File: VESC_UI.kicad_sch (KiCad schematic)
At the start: 60 parts, among them J1 Hall_DRV5055-Q1, J2 Hall_DRV5055-Q1, J3 Conn_01x07_Male, J4 Conn_02x05_Female, J5 Conn_01x05_Male, J6 Conn_01x04_Male, J8 Conn_01x02_Male, J9 Conn_01x02_Male, Q1 Mosfet IRLML2060TRPBF, Q2 Mosfet IRLML2060TRPBF, SW1 Vertical push button, SW2 Vertical push button, SW3 Vertical push button, SW4 Vertical push button, SW5 Push button, U2 STM32F401CEU6, U3 M95M04-DR

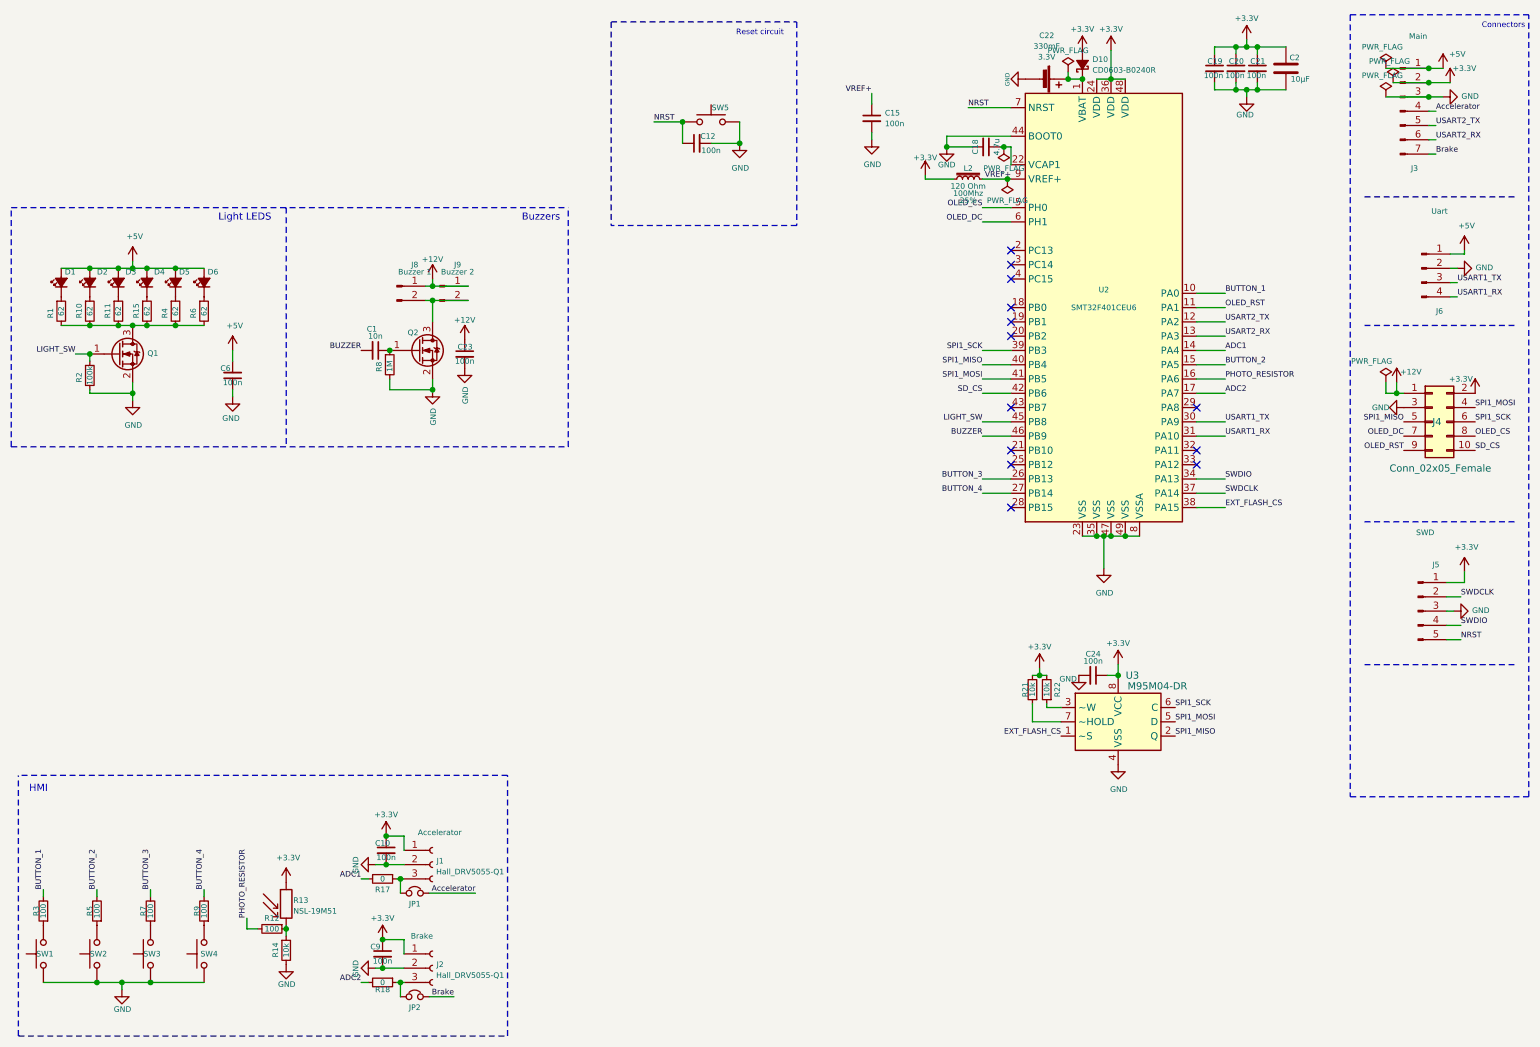
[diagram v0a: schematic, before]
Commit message: Merge display shield and update smd components case
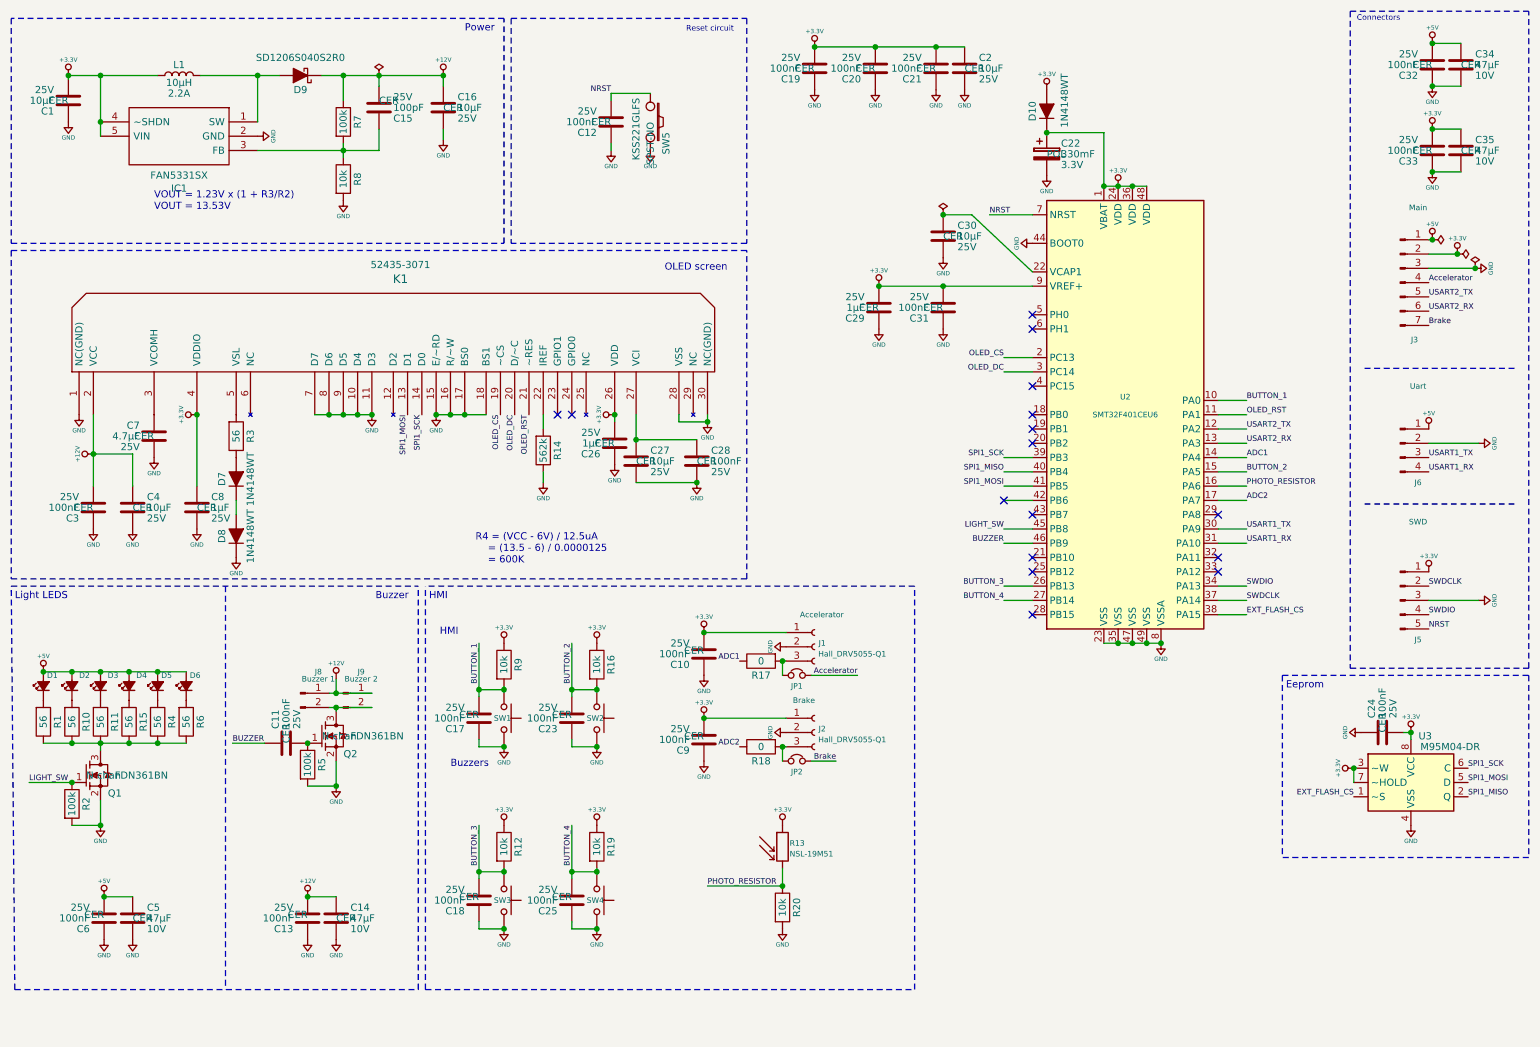
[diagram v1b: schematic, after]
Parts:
- removed C1: 10n, Capacitor_SMD:C_0603_1608Metric_Pad1.05x0.95mm_HandSolder, symbol Device:C_Small
- removed C10, C12, C15, C19, C20, C21, C23, C24, C6, C9: 100n, Capacitor_SMD:C_0603_1608Metric_Pad1.05x0.95mm_HandSolder, symbol Device:C_Small
- removed C18: 4.7u, Capacitor_SMD:C_0603_1608Metric_Pad1.05x0.95mm_HandSolder, symbol Device:C_Small
- removed C2: 10µF, Capacitor_SMD:C_0805_2012Metric_Pad1.15x1.40mm_HandSolder, symbol Device:C
- removed C22: SUpercap 330mF, SamacSys_Parts:DSK3R3H334THL, symbol Device:Battery_Cell
- removed D10: Schottky CD0603-B0240R, Diode_SMD:D_0603_1608Metric_Pad1.05x0.95mm_HandSolder, symbol VESC_UI-rescue:D_Schottky_Small_ALT-Device
- removed J4: Conn_02x05_Female, Connector_PinSocket_2.00mm:PinSocket_2x05_P2.00mm_Vertical, symbol Connector_Generic:Conn_02x05_Odd_Even
- removed L2: MMZ1608B121CTDH5, Inductor_SMD:L_0603_1608Metric_Pad1.05x0.95mm_HandSolder, symbol VESC_UI-rescue:L_Core_Iron_Small-Device
- removed Q1, Q2: Mosfet IRLML2060TRPBF, Package_TO_SOT_SMD:SOT-23, symbol Transistor_FET:IRLML2060
- removed R1, R10, R11, R15, R4, R6: 62, Resistor_SMD:R_0603_1608Metric_Pad1.05x0.95mm_HandSolder, symbol Device:R_Small
- removed R12, R3, R5, R7, R9: 100, Resistor_SMD:R_0603_1608Metric_Pad1.05x0.95mm_HandSolder, symbol Device:R_Small
- removed R14, R21, R22: 10k, Resistor_SMD:R_0603_1608Metric_Pad1.05x0.95mm_HandSolder, symbol Device:R_Small
- removed R17, R18: 0, Resistor_SMD:R_0603_1608Metric_Pad1.05x0.95mm_HandSolder, symbol Device:R_Small
- removed R2: 100k, Resistor_SMD:R_0603_1608Metric_Pad1.05x0.95mm_HandSolder, symbol Device:R_Small
- removed R8: 1M, Resistor_SMD:R_0603_1608Metric_Pad1.05x0.95mm_HandSolder, symbol Device:R_Small
- removed SW5: Push button, Button_Switch_SMD:SW_SPST_B3U-1000P-B, symbol Switch:SW_Push
- added C1, C16, C2, C27, C30, C4: C_0003, DVB_Capacitors_Ceramic:C_0603, symbol DVB_C:C_0003
- added C10, C11, C12, C13, C17, C18, C19, C20, C21, C23, C24, C25, C28, C3, C31, C32, C33, C6, C9: C_0002, DVB_Capacitors_Ceramic:C_0402, symbol DVB_C:C_0002
- added C14, C34, C35, C5: C_0040, DVB_Capacitors_Ceramic:C_1210, symbol DVB_C:C_0040
- added C15: C_0051, DVB_Capacitors_Ceramic:C_0402, symbol DVB_C:C_0051
- added C22: C_0046, DVB_Capacitors_Supercap:CP_ELNA-DSK621, symbol DVB_C:C_0046
- added C26, C29, C8: C_0037, DVB_Capacitors_Ceramic:C_0603, symbol DVB_C:C_0037
- added C7: C_0036, DVB_Capacitors_Ceramic:C_0603, symbol DVB_C:C_0036
- added D10, D7, D8: D_0022, DVB_Diodes:D_SOD-523-F, symbol DVB_D:D_0022
- added D9: D_0016, DVB_Diodes:D_SOD-123, symbol DVB_D:D_0016
- added IC1: FAN5331SX, SOT95P280X145-5N, symbol SamacSys_Parts:FAN5331SX
- added K1: K_0051-OBSOLETE, DVB_Displays:OLED128x128-1P5, symbol DVB_K:K_0051-OBSOLETE
- added L1: L_0006, DVB_Inductors:L_4012-Wurth, symbol DVB_L:L_0006
- added Q1, Q2: Q_0020, DVB_SOT:SOT_23, symbol DVB_Q:Q_0020
- added R1, R10, R11, R15, R3, R4, R6: R_0110, DVB_Resistors:R_0402, symbol DVB_R:R_0110
- added R12, R16, R19, R20, R8, R9: R_0020, DVB_Resistors:R_0402, symbol DVB_R:R_0020
- added R14: R_0019, DVB_Resistors:R_0402, symbol DVB_R:R_0019
- added R17, R18: R_0001, DVB_Resistors:R_0402, symbol DVB_R:R_0001
- added R2, R5, R7: R_0034, DVB_Resistors:R_0402, symbol DVB_R:R_0034
- added SW5: SW_0002, DVB_Buttons:KSS221G, symbol DVB_SW:SW_0002
- U2: value STM32F401CEU6 -> STM32F401CEUx
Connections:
- net +3V3 is gone; now on net +3.3V: J1.1 (Pin_1), J2.1 (Pin_1), J3.2 (Pin_2), J5.1 (Pin_1), R13.1, U2.24 (VDD), U2.36 (VDD), U2.48 (VDD), U3.8 (VCC)
- net VREF+ is gone; now on net +3.3V: U2.9 (VREF+)
- net +12V: now also C13.2, C14.1, C15.2, C16.1, C3.2, C4.1, D9.1 (K), K1.2 (VCC), R7.2
- net +5V: now also C32.2, C34.1, C5.1, C6.2
- net ADC1: now also R17.2
- net ADC2: now also R18.2
- net BUTTON_1: now also SW1.1, C17.2, R9.1
- net BUTTON_2: now also SW2.1, C23.2, R16.1
- net BUTTON_3: now also SW3.1, C18.2, R12.1
- net BUTTON_4: now also SW4.1, C25.2, R19.1
- net BUZZER: now also C11.1
- net GND: now also SW1.2, SW2.2, SW3.2, SW4.2, C1.1, C10.1, C12.1, C13.1, C14.2, C16.2, C17.1, C18.1, C19.1, C2.2, C20.1, C21.1, C22.2, C23.1, C24.1, C25.1, C26.1, C27.2, C28.2, C29.1, C3.1, C30.2, C31.1, C32.1, C33.1, C34.2, C35.2, C4.2, C5.2, C6.1, C7.2, C8.2, C9.1, D8.1 (K), IC1.2 (GND), K1.1 (NC(GND)), K1.10 (D4), K1.11 (D3), K1.15 (E/~RD), K1.16 (R/~W), K1.17 (BS0), K1.18 (BS1), K1.28 (VSS), K1.30 (NC(GND)), K1.7 (D7), K1.8 (D6), K1.9 (D5), Q1.2 (S), Q2.2 (S), R14.2, R2.1, R20.1, R5.1, R8.1, SW5.2; no longer SW1.1, SW2.1, SW3.1, SW4.1
- net LIGHT_SW: now also Q1.1 (G), R2.2
- net NRST: now also C12.2, SW5.1
- net OLED_CS: now also U2.2 (PC13), K1.19 (~CS); no longer U2.5 (PH0)
- net OLED_DC: now also U2.3 (PC14), K1.20 (D/~C); no longer U2.6 (PH1)
- net OLED_RST: now also K1.21 (~RES)
- net PHOTO_RESISTOR: now also R13.2, R20.2
- net SPI1_MOSI: now also K1.13 (D1)
- net SPI1_SCK: now also K1.14 (D0)
- net +3.3V: now reaches U2.1 (VBAT)
- net +3.3V: now also U3.3 (~W), U3.7 (~HOLD), C1.2, C10.2, C19.2, C2.1, C20.2, C21.2, C22.1, C24.2, C26.2, C29.2, C31.2, C33.2, C35.1, C8.1, C9.2, D10.1 (K), D10.2 (A), IC1.4 (~SHDN), IC1.5 (VIN), K1.26 (VDD), K1.4 (VDDIO), L1.2, R12.2, R16.2, R19.2, R9.2
- net at U2.22 (VCAP1): now also C30.1
- net at D1.1 (K): now also R1.1
- net at D2.1 (K): now also R10.1
- net at D3.1 (K): now also R11.1
- net at D4.1 (K): now also R15.1
- net at D5.1 (K): now also R4.1
- net at D6.1 (K): now also R6.1
- net at J2.3 (Pin_3), JP2.1: now also R18.1
- net at J1.3 (Pin_3), JP1.1: now also R17.1
- net at J8.2 (Pin_2), J9.2 (Pin_2): now also Q2.3 (D)
- net SD_CS: no longer names the net of U2.42 (PB6)
- new net: K1.5 (VSL), R3.1
- new net: D7.2 (A), R3.2
- new net: Q1.3 (D), R1.2, R10.2, R11.2, R15.2, R4.2, R6.2
- new net: C27.1, C28.1, K1.27 (VCI)
- new net: D7.1 (K), D8.2 (A)
- new net: C11.2, Q2.1 (G), R5.2
- new net: C15.1, IC1.3 (FB), R7.1, R8.2
- new net: C7.1, K1.3 (VCOMH)
- new net: K1.22 (IREF), R14.1
- new net: D9.2 (A), IC1.1 (SW), L1.1
- no-connect marks 13 -> 16
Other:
- note added: "Buzzer"
- note added: "Eeprom"
- note added: "OLED screen"
- note added: "Power"
- note added: "R4 = (VCC - 6V) / 12.5uA = (13.5 - 6) / 0.0000125 = 600K"
- note added: "VOUT = 1.23V x (1 + R3/R2) VOUT = 13.53V"
- moved on the sheet: D1, D2, D3, D4, D5, D6, J1, J2, J3, J5, J6, J8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

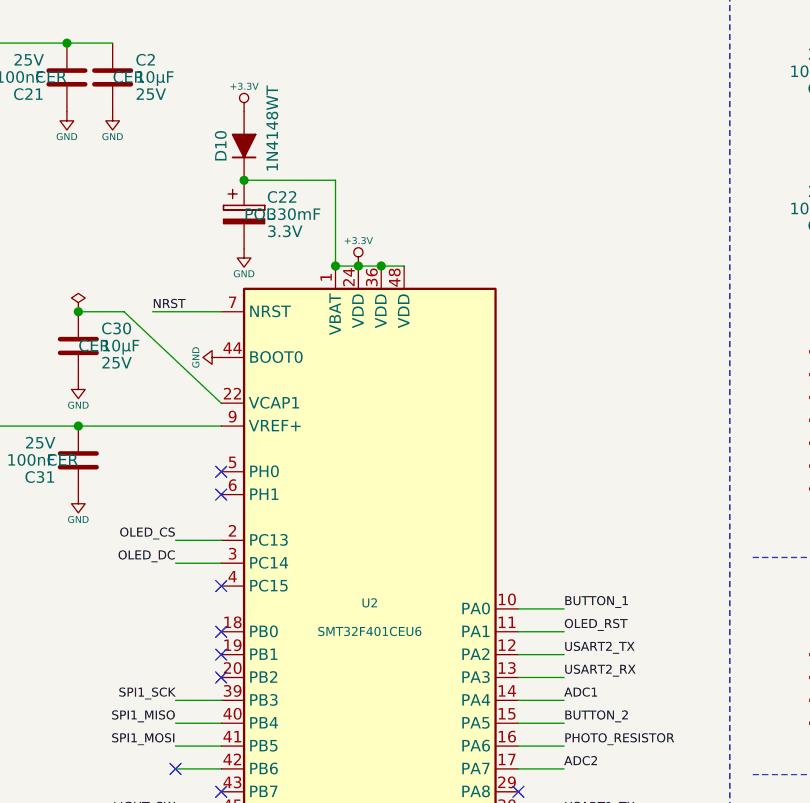
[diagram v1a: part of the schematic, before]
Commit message: Update STM32 lib
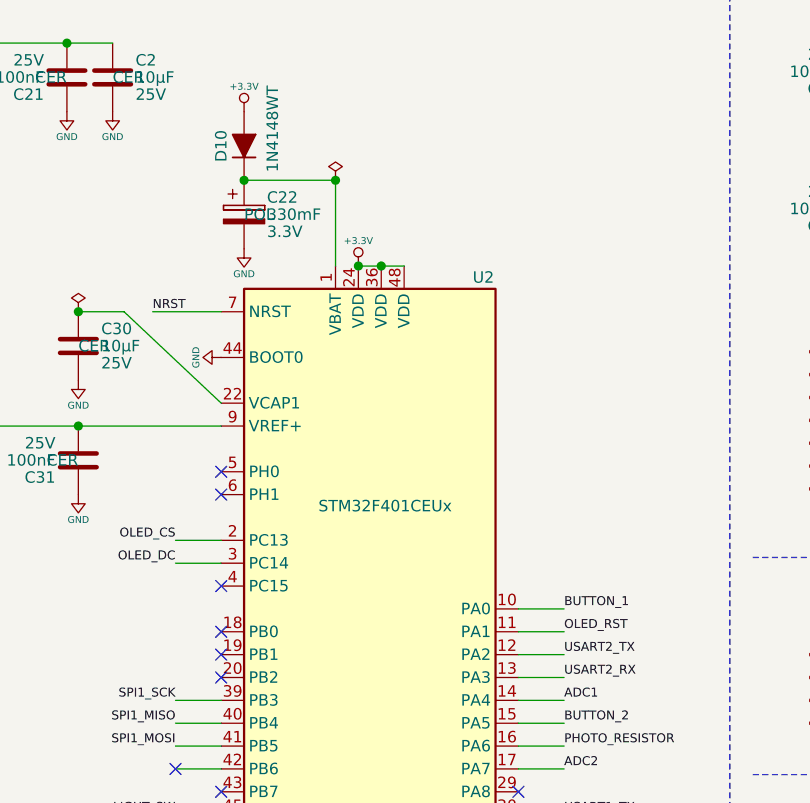
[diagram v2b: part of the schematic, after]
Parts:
- U2: Name SMT32F401CEU6 -> (none)
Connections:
- net +3.3V: no longer C22.1, D10.1 (K), U2.1 (VBAT)
- new net: C22.1, D10.1 (K), U2.1 (VBAT)
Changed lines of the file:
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@@
   (junction (at 179.07 62.865) (diameter 1.016) (color 0 0 0 0))
   (junction (at 197.485 35.56) (diameter 1.016) (color 0 0 0 0))
-  (junction (at 207.645 45.085) (diameter 1.016) (color 0 0 0 0))
+  (junction (at 207.645 35.56) (diameter 1.016) (color 0 0 0 0))
   (junction (at 210.185 45.085) (diameter 1.016) (color 0 0 0 0))
   (junction (at 210.185 126.365) (diameter 1.016) (color 0 0 0 0))
@@
     (stroke (width 0) (type solid) (color 0 0 0 0))
   )
-  (wire (pts (xy 207.645 45.085) (xy 210.185 45.085))
-    (stroke (width 0) (type solid) (color 0 0 0 0))
-  )
   (wire (pts (xy 207.645 126.365) (xy 210.185 126.365))
     (stroke (width 0) (type solid) (color 0 0 0 0))
@@
     (pin "1")
   )
+  (symbol (lib_id "DVB_Power:P_FLG") (at 207.645 35.56 0) (unit 1)
+    (in_bom yes) (on_board yes)
+    (property "Reference" "#FLG0103" (id 0) (at 207.645 36.83 0)
+      (effects (font (size 0.762 0.762)) hide)
+    )
+    (property "Value" "P_FLG" (id 1) (at 207.645 32.766 0)
+      (effects (font (size 0.762 0.762)) hide)
+    )
+    (property "Footprint" "" (id 2) (at 207.645 35.56 0)
+      (effects (font (size 1.27 1.27)) hide)
+    )
+    (property "Datasheet" "" (id 3) (at 207.645 35.56 0)
+      (effects (font (size 1.27 1.27)) hide)
+    )
+    (pin "1")
+  )
   (symbol (lib_id "DVB_Power:GND") (at 217.805 126.365 0) (unit 1)
     (in_bom yes) (on_board yes)
@@
     (pin "9")
   )
-  (symbol (lib_id "MCU_ST_STM32F4:STM32F401CEUx") (at 212.725 85.725 0) (unit 1)
+  (symbol (lib_name "MCU_ST_STM32F4:STM32F401CEUx_1") (lib_id "MCU_ST_STM32F4:STM32F401CEUx") (at 212.725 85.725 0) (unit 1)
     (in_bom yes) (on_board yes)
-    (property "Reference" "U2" (id 0) (at 211.455 82.55 0)
-      (effects (font (size 0.9906 0.9906)))
+    (property "Reference" "U2" (id 0) (at 222.885 46.355 0)
+      (effects (font (size 1.27 1.27)) (justify left))
     )
-    (property "Value" "STM32F401CEUx" (id 1) (at 211.455 42.799 0)
-      (effects (font (size 0.9906 0.9906)) hide)
+    (property "Value" "STM32F401CEUx" (id 1) (at 205.74 71.755 0)
+      (effects (font (size 1.27 1.27)) (justify left))
     )
     (property "Footprint" "Package_DFN_QFN:QFN-48-1EP_7x7mm_P0.5mm_EP5.6x5.6mm" (id 2) (at 197.485 123.825 0)
-      (effects (font (size 0.9906 0.9906)) (justify right) hide)
+      (effects (font (size 1.27 1.27)) (justify right) hide)
     )
     (property "Datasheet" "http://www.st.com/st-web-ui/static/active/en/resource/technical/document/datasheet/DM00102166.pdf" (id 3) (at 212.725 85.725 0)
-      (effects (font (size 0.9906 0.9906)) hide)
-    )
-    (property "Name" "SMT32F401CEU6" (id 4) (at 211.455 85.725 0)
-      (effects (font (size 0.9906 0.9906)))
+      (effects (font (size 1.27 1.27)) hide)
     )
     (pin "1")
@@
       (reference "#FLG0102") (unit 1) (value "P_FLG") (footprint "")
     )
+    (path "/6a28c7d6-b316-4eab-80cd-3af31f5a8b1a"
+      (reference "#FLG0103") (unit 1) (value "P_FLG") (footprint "")
+    )
     (path "/a3475c92-5fc1-4598-99e0-e74c1a3c0432"
       (reference "#PWR01") (unit 1) (value "+5V") (footprint "")
@@
       (reference "SW5") (unit 1) (value "SW_0002") (footprint "DVB_Buttons:KSS221G")
     )
-    (path "/bf300d7d-197d-4a9c-a9eb-4ceae38cfae9"
+    (path "/6d0ff79b-0241-4693-a6ac-4fd600ca2613"
       (reference "U2") (unit 1) (value "STM32F401CEUx") (footprint "Package_DFN_QFN:QFN-48-1EP_7x7mm_P0.5mm_EP5.6x5.6mm")
     )
